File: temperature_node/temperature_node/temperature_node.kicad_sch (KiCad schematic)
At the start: 11 parts, among them J1 USB_C_Receptacle_USB2.0_16P, U1 ESP32-C3-WROOM-02, U2 SHT4x, U3 MCP73831-2-OT, U4 MIC5504-3.3YM5, U5 AP9101CK

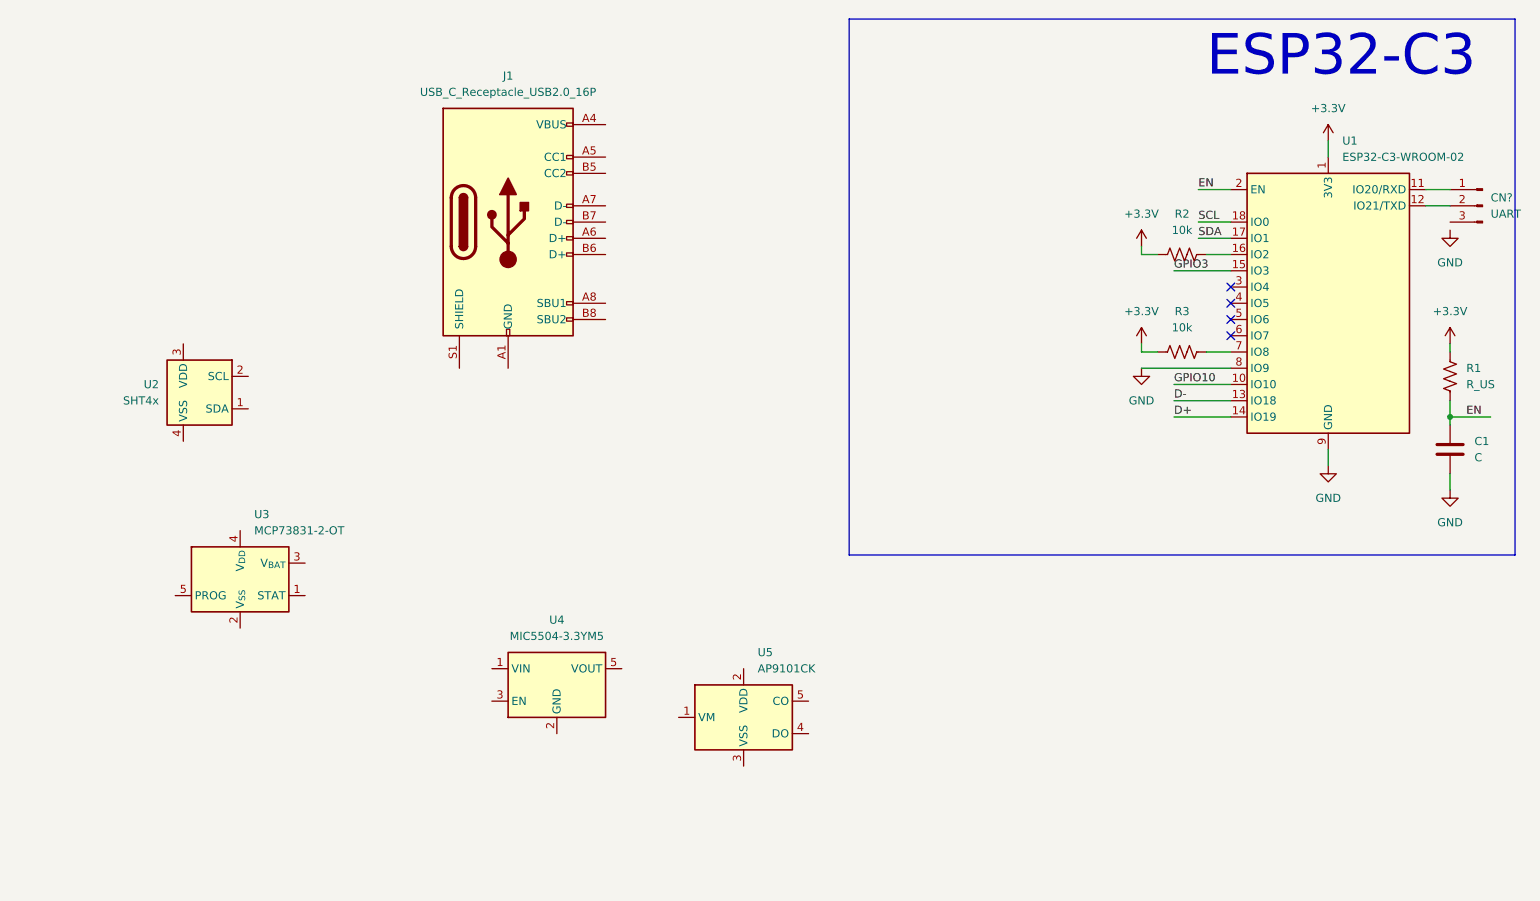
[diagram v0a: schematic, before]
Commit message: Connect USB and SHT40
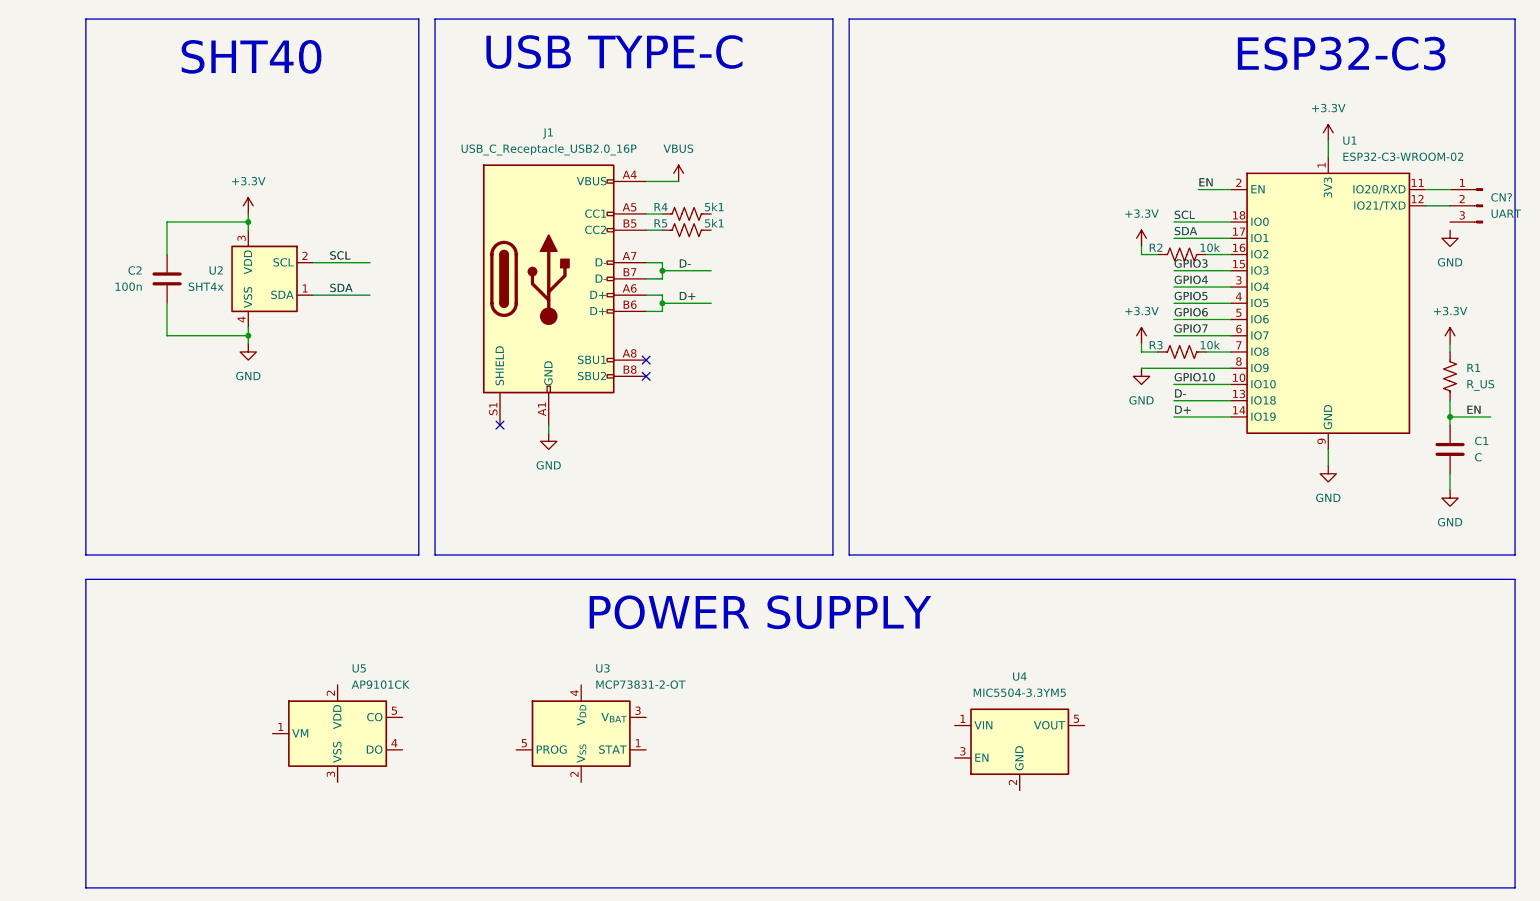
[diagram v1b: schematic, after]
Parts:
- added C2: 100n, Capacitor_SMD:C_0402_1005Metric, symbol Device:C
- added R4, R5: 5k1, Resistor_SMD:R_0402_1005Metric, symbol Device:R_US
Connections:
- net +3.3V: now also U2.3 (VDD), C2.1
- net D+: now also J1.A6 (D+), J1.B6 (D+)
- net D-: now also J1.A7 (D-), J1.B7 (D-)
- net GND: now also J1.A1 (GND), J1.A12 (GND), J1.B1 (GND), J1.B12 (GND), U2.4 (VSS), C2.2
- net SCL: now also U2.2 (SCL)
- net SDA: now also U2.1 (SDA)
- net GPIO4: now reaches U1.3 (IO4)
- net GPIO5: now reaches U1.4 (IO5)
- net GPIO6: now reaches U1.5 (IO6)
- net GPIO7: now reaches U1.6 (IO7)
- net VBUS: now reaches J1.A4 (VBUS), J1.A9 (VBUS), J1.B4 (VBUS), J1.B9 (VBUS)
- net at J1.A5 (CC1): now also R4.2
- net at J1.B5 (CC2): now also R5.2
- no-connect marks 4 -> 3
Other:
- note added: "POWER SUPPLY"
- note added: "SHT40"
- note added: "USB TYPE-C"
- moved on the sheet: J1, U2, U3, U4, U5

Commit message: Finish pre stock review schematics
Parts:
- removed U5: AP9101CK, Package_TO_SOT_SMD:SOT-23-5, symbol Battery_Management:AP9101CK
- added C2, C3: 4u7, Capacitor_SMD:C_0402_1005Metric, symbol Device:C
- added C4, C5: 1u, Capacitor_SMD:C_0402_1005Metric, symbol Device:C
- added C7: 10u, Capacitor_SMD:C_0402_1005Metric, symbol Device:C
- added C8: 100n, Capacitor_SMD:C_0402_1005Metric, symbol Device:C
- added D1: 1.5SMC6.8CA, Diode_SMD:D_SMC, symbol Diode:1.5SMCxxCA
- added D2: APA102, LED_SMD:LED_RGB_5050-6, symbol LED:APA102
- added J2: S2B-PH-K-S, Connector_JST:JST_PH_S2B-PH-K_1x02_P2.00mm_Horizontal, symbol Connector_Generic:Conn_01x02
- added JP1: ~, Jumper:SolderJumper-2_P1.3mm_Open_RoundedPad1.0x1.5mm, symbol Jumper:SolderJumper_2_Open
- added R1, R2, R4: 10k, Resistor_SMD:R_0402_1005Metric, symbol Device:R_US
- added R11, R12: 100k, Resistor_SMD:R_0402_1005Metric, symbol Device:R_US
- added R3: 4k7, Resistor_SMD:R_0402_1005Metric, symbol Device:R_US
- C6: renamed from C1; value C -> 1u
- R10: renamed from R1; value R_US -> 10k
- U1: renamed from U2; value SHT4x -> SHT40-AD1B-R3
- gave numbers to parts that had none: 1
- renumbered C2 to C1, R4 to R5, R5 to R6, R2 to R8, R3 to R9, U3 to U2, U4 to U3, U1 to U4
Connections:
- net GPIO10 is gone; now on net CHG_STAT: U4.10 (IO10)
- net +3.3V: now also U3.5 (VOUT), C5.1, C7.1, C8.1, D2.4 (VCC); no longer C1.1, U1.3 (VDD)
- net GND: now also CN1.3 (Pin_3), R5.1, R6.1, U2.2 (V_{SS}), U3.2 (GND), C2.2, C3.2, C4.2, C5.2, C7.2, C8.2, D1.1 (A1), D2.3 (GND), J2.2 (Pin_2), JP1.1 (A), R12.2, R3.2; no longer U4.8 (IO9)
- net SCL: now also R1.2
- net SDA: now also R2.2
- net VBUS: now also U2.4 (V_{DD}), C2.1, D1.2 (A2)
- net CHG_STAT: now reaches U2.1 (STAT)
- net CHG_STAT: now also R4.2
- net +BATT: now reaches U2.3 (V_{BAT})
- net +BATT: now also U3.1 (VIN), U3.3 (EN), C3.1, C4.1, J2.1 (Pin_1), R11.1, R4.1
- net at U2.5 (PROG): now also R3.1
- net GPIO3 renamed BATT
- net BATT: now also R11.2, R12.1
- net GPIO4 renamed LED_DI
- net LED_DI: now also D2.1 (DI)
- net GPIO5 renamed LED_CI
- net LED_CI: now also D2.2 (CI)
- net GPIO6 renamed SHT_EN
- net SHT_EN: now also C1.1, U1.3 (VDD), R1.1, R2.1
- new net: JP1.2 (B), U4.8 (IO9)
- no-connect marks 3 -> 6
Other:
- note added: "RGB LED"
- moved on the sheet: C6, R10, U2, U3

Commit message: Add notes to SCH and review pre PCB design
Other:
- note added: "${TITLE}"
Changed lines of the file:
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@@
+		)
+	)
+	(text "${TITLE}"
+		(exclude_from_sim no)
+		(at 189.484 190.5 0)
+		(effects
+			(font
+				(size 1.27 1.27)
+				(color 0 0 0 1)
+			)
 		)
 	)

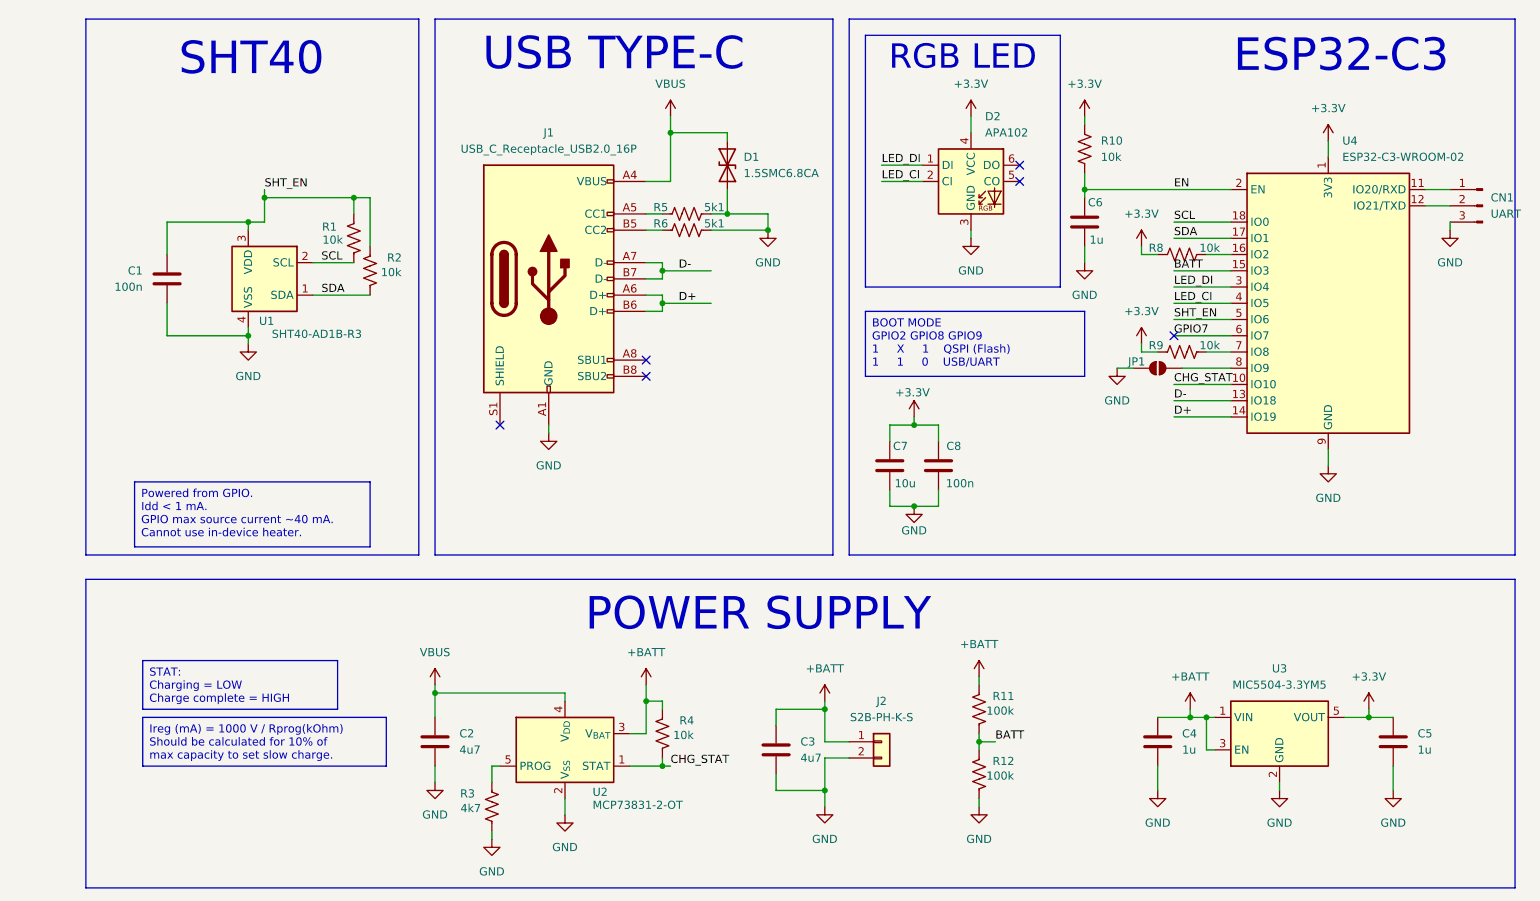
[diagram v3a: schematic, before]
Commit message: Set slow charge to 100 mA with RPROG as 10k
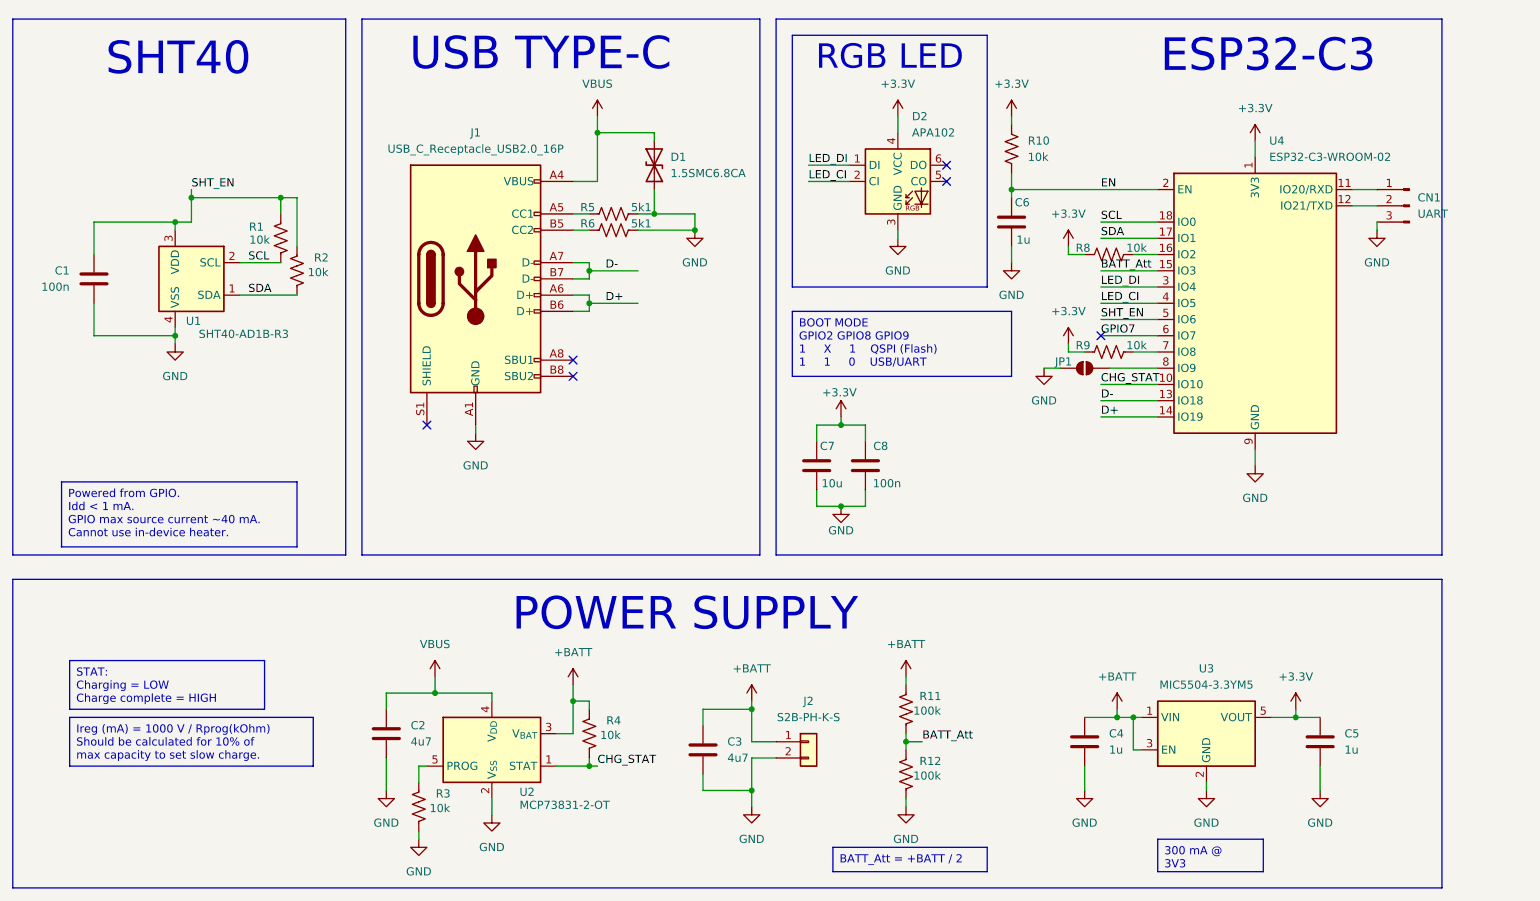
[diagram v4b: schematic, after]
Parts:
- R3: value 4k7 -> 10k
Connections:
- net BATT renamed BATT_Att
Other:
- moved on the sheet: C1, C2, C3, C4, C5, C6, C7, C8, CN1, D1, D2, J1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

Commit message: Use a smaller header for UART connector
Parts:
- CN1: footprint Connector_Wire:SolderWire-2.5sqmm_1x03_P7.2mm_D2.4mm_OD3.6mm -> Connector_Wire:SolderWire-0.1sqmm_1x03_P3.6mm_D0.4mm_OD1mm
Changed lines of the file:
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@@
 			)
 		)
-		(property "Footprint" "Connector_Wire:SolderWire-2.5sqmm_1x03_P7.2mm_D2.4mm_OD3.6mm"
+		(property "Footprint" "Connector_Wire:SolderWire-0.1sqmm_1x03_P3.6mm_D0.4mm_OD1mm"
 			(at 254 53.34 0)
 			(effects

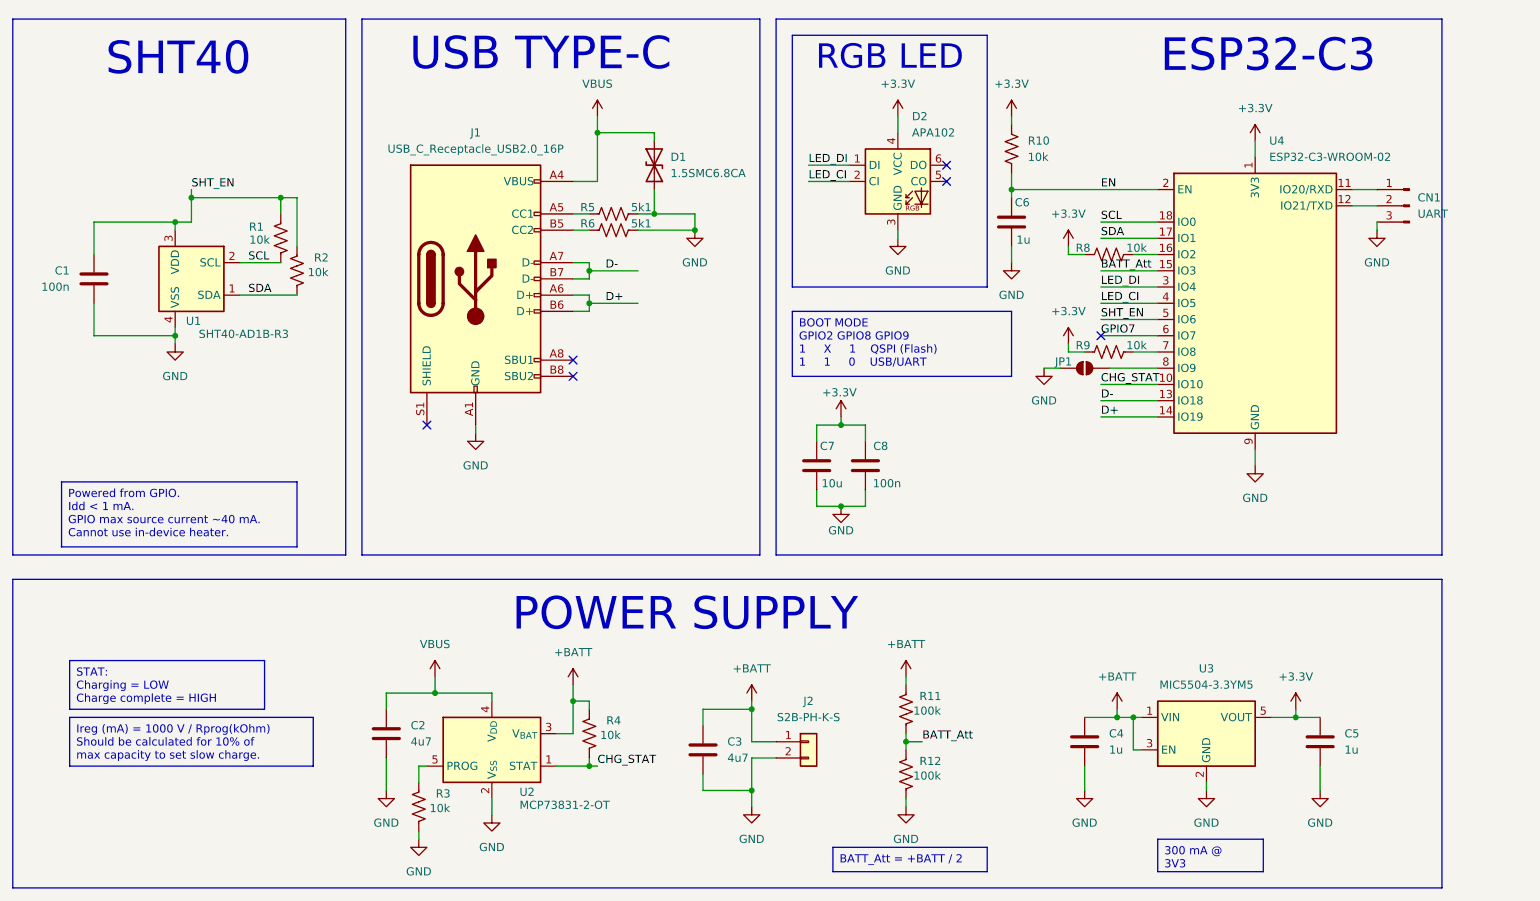
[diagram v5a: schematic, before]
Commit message: Add 1mm PAD test points
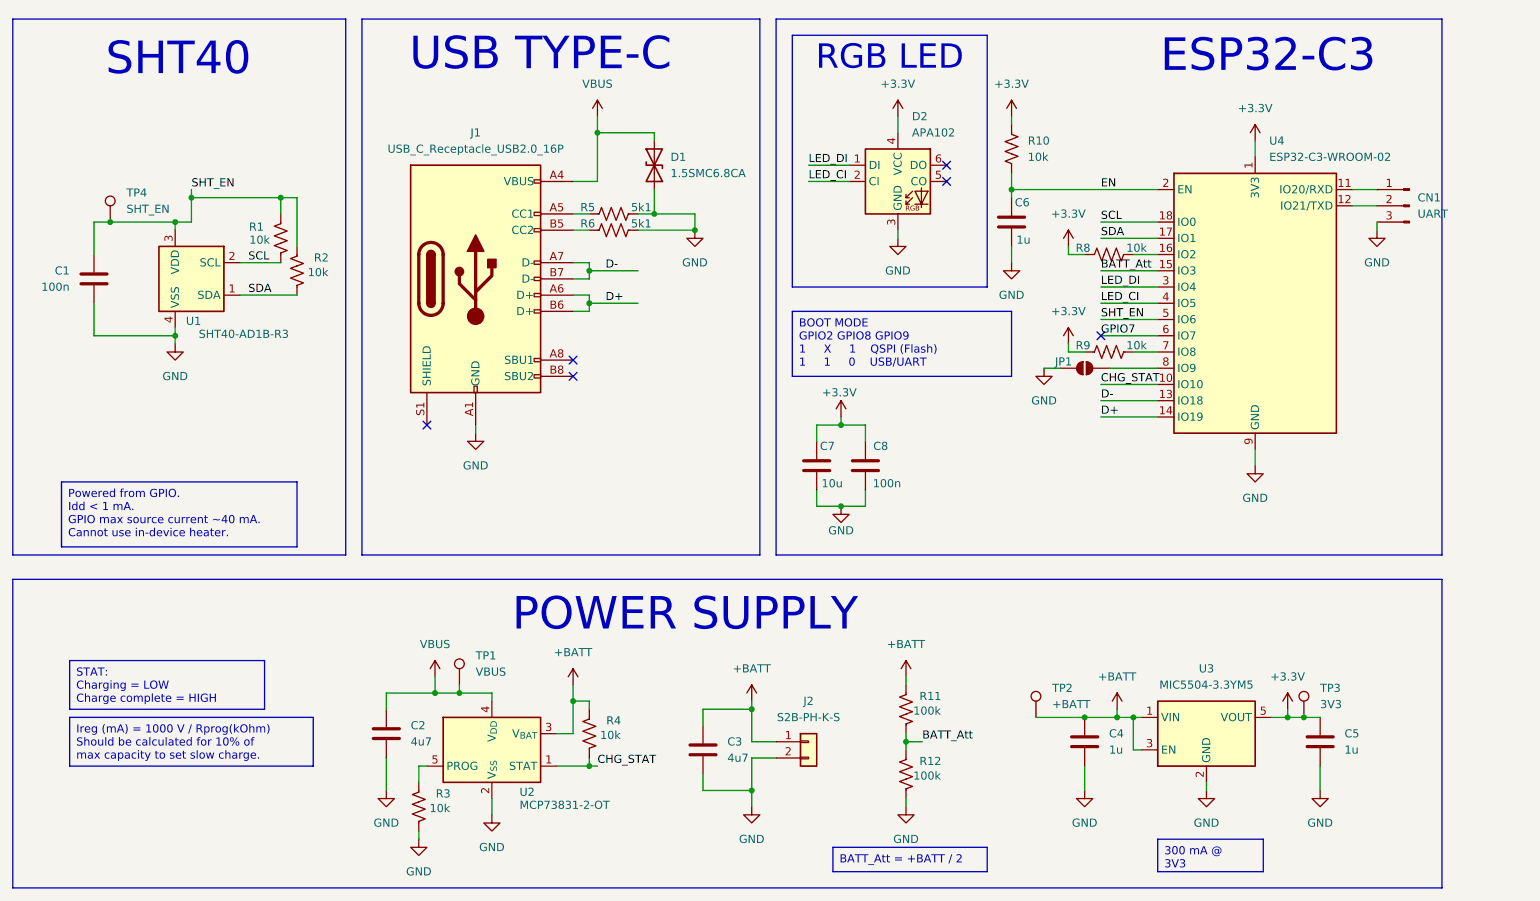
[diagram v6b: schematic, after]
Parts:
- added TP1: VBUS, TestPoint:TestPoint_Pad_D1.0mm, symbol Connector:TestPoint
- added TP2: +BATT, TestPoint:TestPoint_Pad_D1.0mm, symbol Connector:TestPoint
- added TP3: 3V3, TestPoint:TestPoint_Pad_D1.0mm, symbol Connector:TestPoint
- added TP4: SHT_EN, TestPoint:TestPoint_Pad_D1.0mm, symbol Connector:TestPoint
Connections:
- net +3.3V: now also TP3.1
- net +BATT: now also TP2.1
- net SHT_EN: now also TP4.1
- net VBUS: now also TP1.1
